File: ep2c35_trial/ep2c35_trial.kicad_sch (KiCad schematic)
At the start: 175 parts, among them J1 Conn_02x21_Odd_Even, J10 Conn_02x10_Odd_Even, J2 Conn_02x21_Odd_Even, J3 3M_8540-4500PL, J4 USB3_B_Micro_Amphenol_GSB343K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, J5 Conn_02x05_Odd_Even, J6 Conn_01x02_Male, J7 Conn_01x02_Male, J8 Conn_01x02_Male, J9 Conn_01x02_Male, U1 EP2C5F484, U10 SP3003-02UTG, U11 SP3003-02UTG, U12 SP3003-02UTG, U13 SP3003-02UTG, U14 SP3003-02UTG, U15 SP3003-02UTG, U16 SP3003-02UTG, U2 MIC37302, U3 FT600Q-B-T, U4 W25Q16JVSNIQ, U5 MIC39102, U6 MIC49150-1.2, U7 SP3003-02UTG, U8 SP3003-02UTG, U9 SP3003-02UTG, X1 FNETHE025, Y1 ABM7-30.000MHZ-D2Y-T

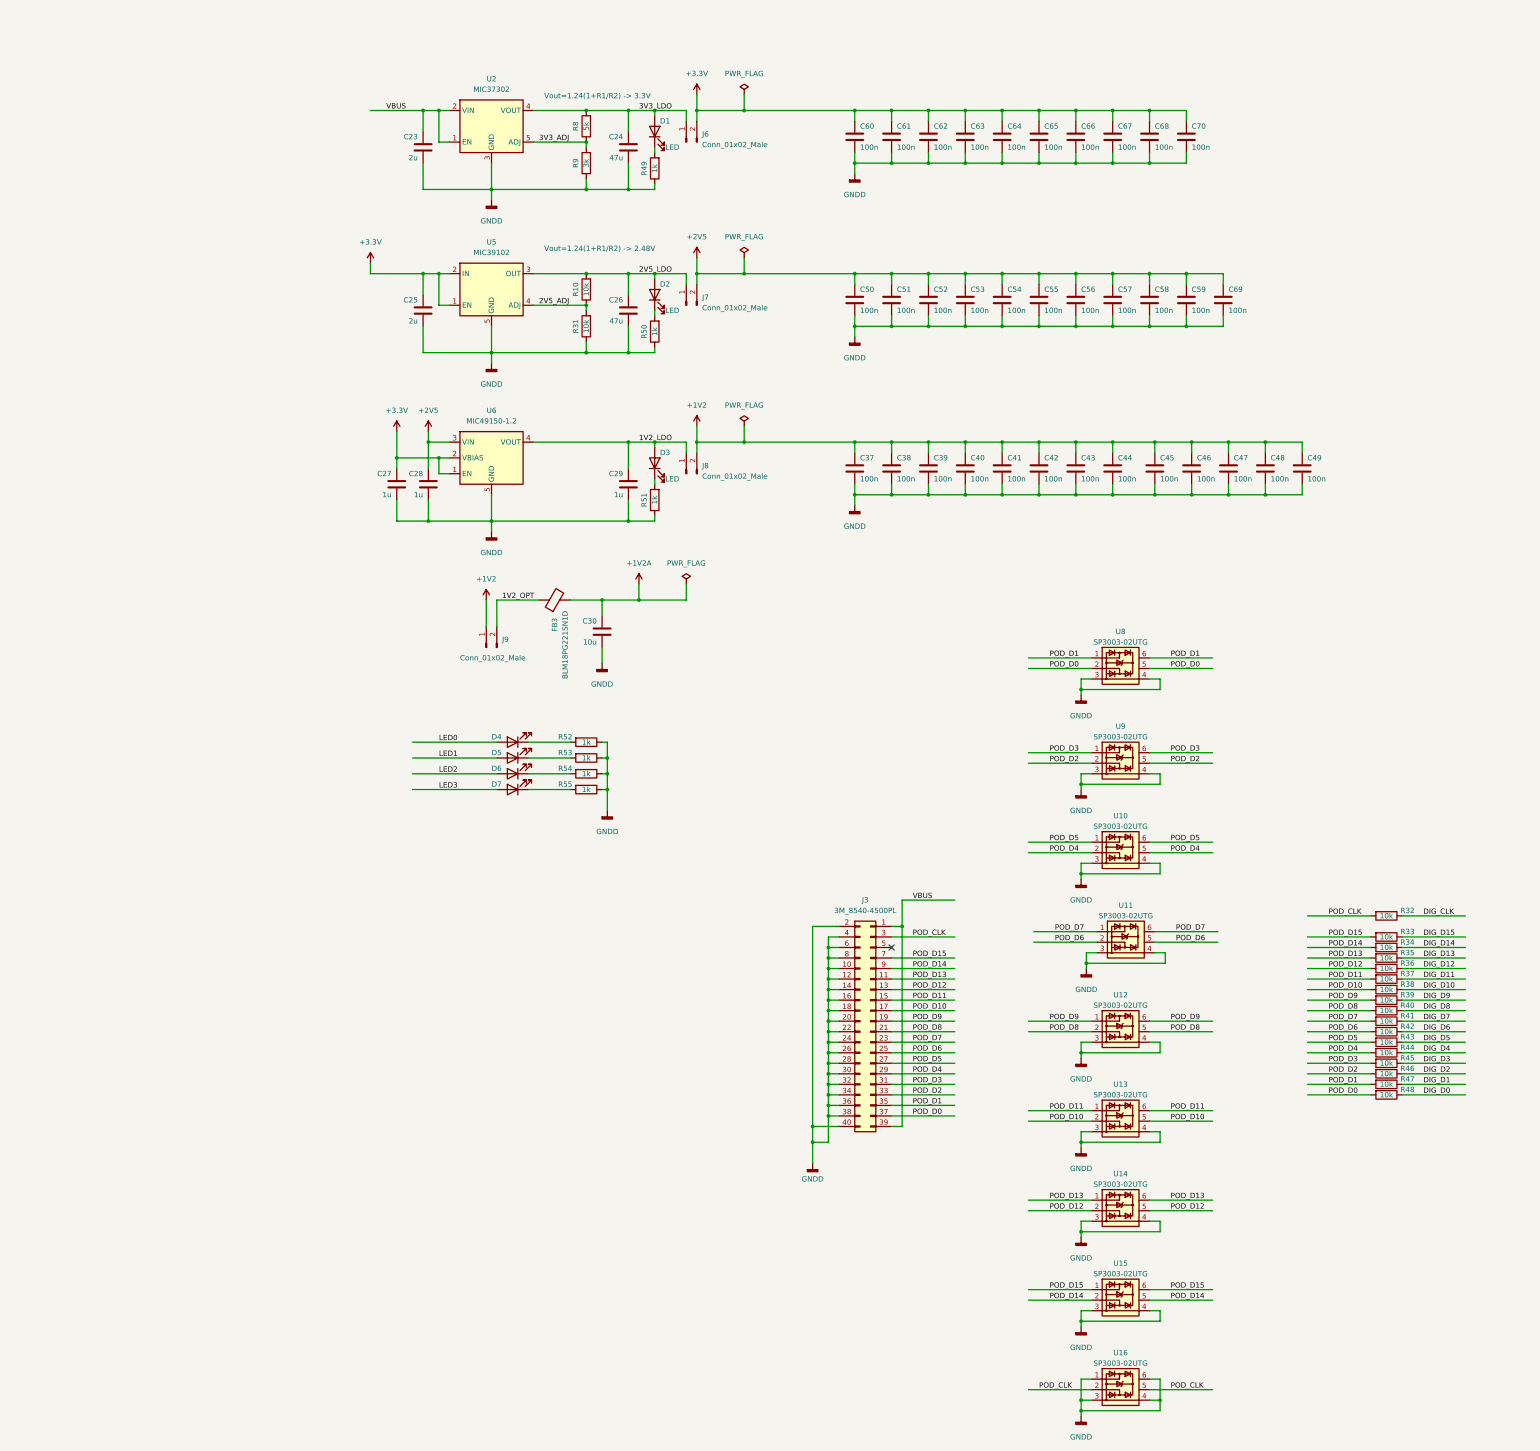
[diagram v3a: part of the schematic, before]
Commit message: Add LM317A power regulators.
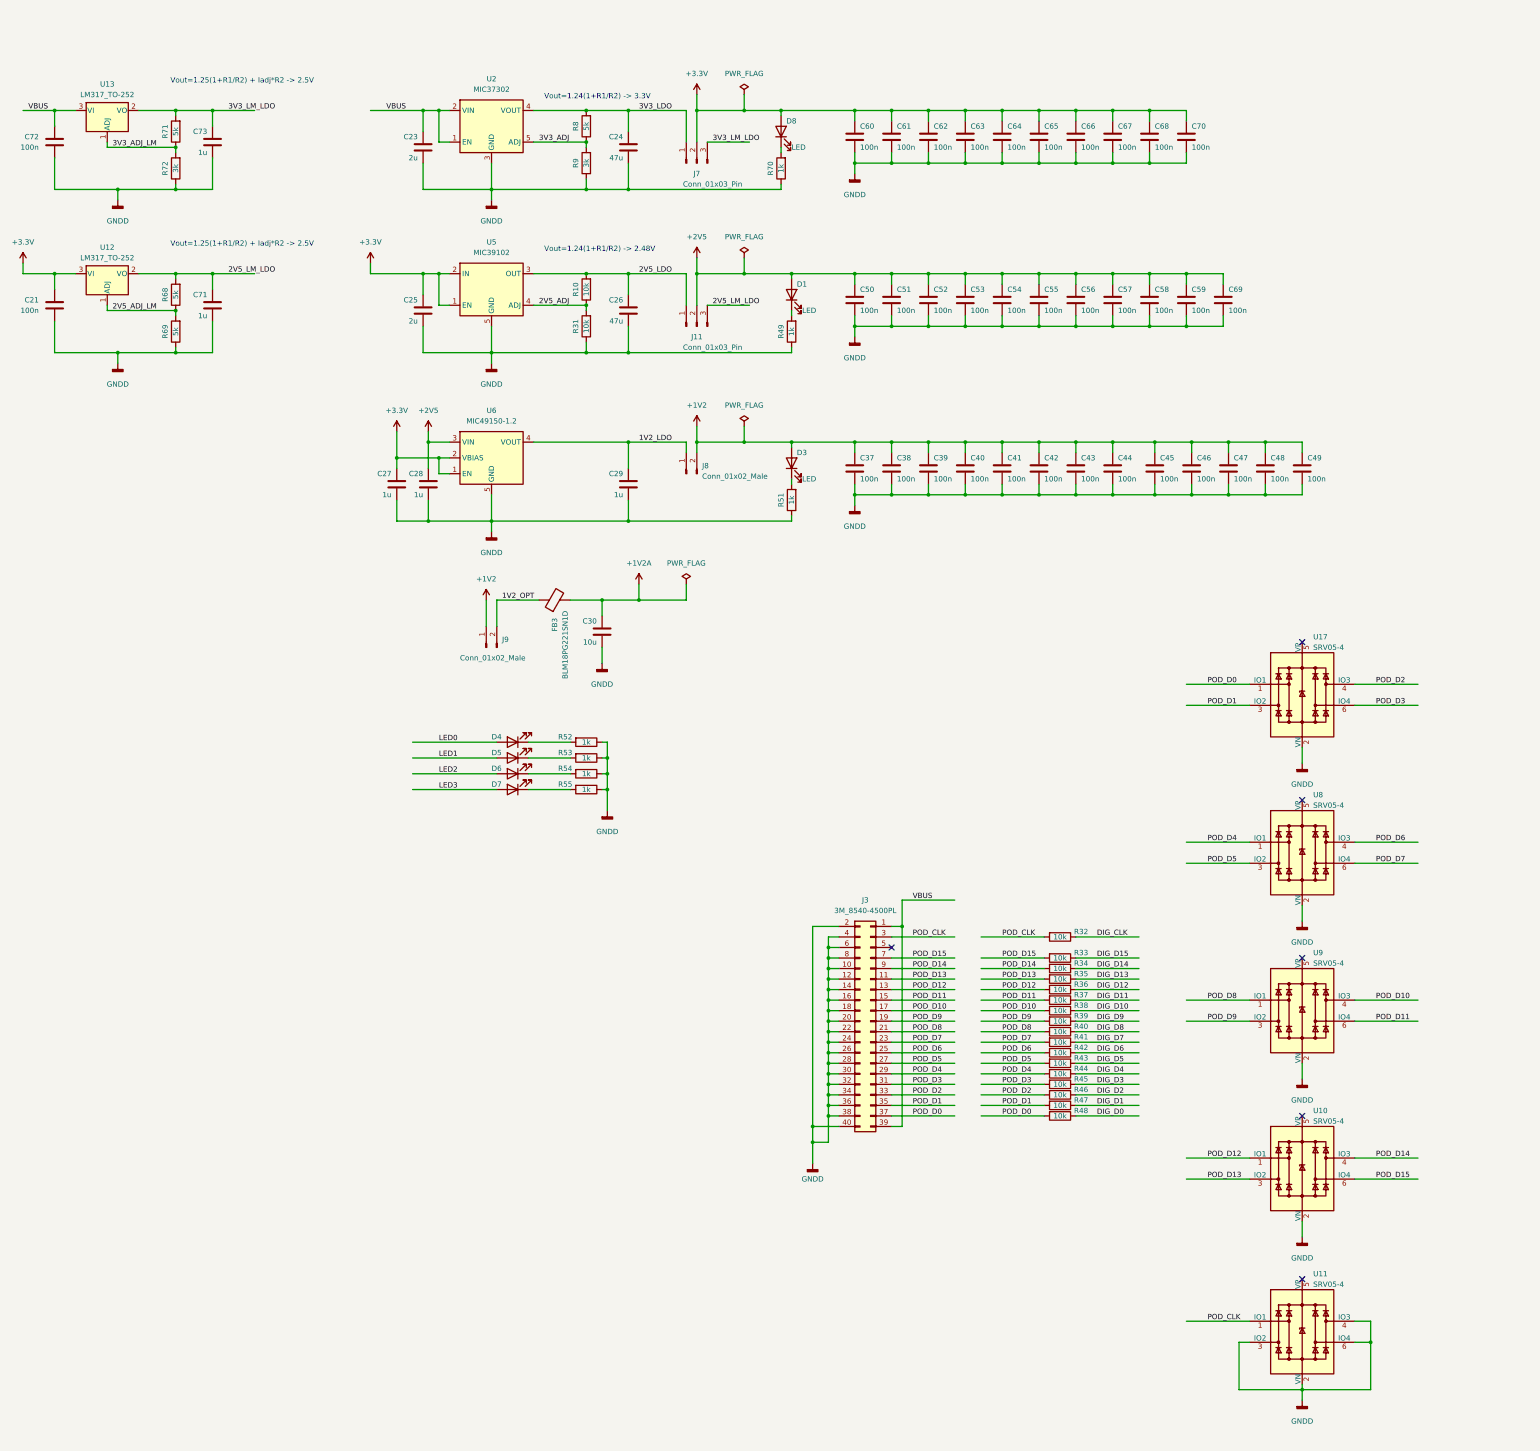
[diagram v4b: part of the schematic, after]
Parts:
- removed D2: LED, LED_SMD:LED_0603_1608Metric, symbol Device:LED
- removed J6, J7: Conn_01x02_Male, Connector_PinHeader_2.54mm:PinHeader_1x02_P2.54mm_Vertical, symbol Connector:Conn_01x02_Male
- removed R50: 1k, Resistor_SMD:R_0402_1005Metric, symbol Device:R
- removed U10, U11, U12, U13, U14, U15, U16, U8, U9: SP3003-02UTG, Package_TO_SOT_SMD:SOT-23-6, symbol logic_analyzer:SP3003-02UTG
- added C21, C72: 100n, Capacitor_SMD:C_0402_1005Metric, symbol Device:C
- added C71, C73: 1u, Capacitor_SMD:C_0805_2012Metric, symbol Device:C
- added D8: LED, LED_SMD:LED_0603_1608Metric, symbol Device:LED
- added J11, J7: Conn_01x03_Pin, Connector_PinHeader_2.54mm:PinHeader_1x03_P2.54mm_Vertical, symbol Connector:Conn_01x03_Pin
- added R68, R69, R71: 5k, Resistor_SMD:R_0402_1005Metric, symbol Device:R
- added R70: 1k, Resistor_SMD:R_0402_1005Metric, symbol Device:R
- added R72: 3k, Resistor_SMD:R_0402_1005Metric, symbol Device:R
- added U10, U11, U17, U8, U9: SRV05-4, Package_TO_SOT_SMD:SOT-23-6, symbol Power_Protection:SRV05-4
- added U12, U13: LM317_TO-252, Package_TO_SOT_SMD:TO-252-2, symbol Regulator_Linear:LM317_TO-252
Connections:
- net +1V2: now also D3.2 (A)
- net +2V5: now also D1.2 (A), J11.2 (Pin_2)
- net +3.3V: now also C21.1, D8.2 (A), J7.2 (Pin_2), U12.3 (VI)
- net 1V2_LDO: no longer D3.2 (A)
- net 2V5_LDO: now also J11.1 (Pin_1)
- net 3V3_LDO: now also J7.1 (Pin_1); no longer D1.2 (A)
- net GND: now also C21.2, C71.1, C72.2, C73.1, R69.1, R70.1, R72.1, U10.2 (VN), U11.2 (VN), U11.3 (IO2), U11.4 (IO3), U11.6 (IO4), U17.2 (VN), U8.2 (VN), U9.2 (VN)
- net POD_CLK: now also U11.1 (IO1)
- net POD_D0: now also U17.1 (IO1)
- net POD_D1: now also U17.3 (IO2)
- net POD_D10: now also U9.4 (IO3)
- net POD_D11: now also U9.6 (IO4)
- net POD_D12: now also U10.1 (IO1)
- net POD_D13: now also U10.3 (IO2)
- net POD_D14: now also U10.4 (IO3)
- net POD_D15: now also U10.6 (IO4)
- net POD_D2: now also U17.4 (IO3)
- net POD_D3: now also U17.6 (IO4)
- net POD_D4: now also U8.1 (IO1)
- net POD_D5: now also U8.3 (IO2)
- net POD_D6: now also U8.4 (IO3)
- net POD_D7: now also U8.6 (IO4)
- net POD_D8: now also U9.1 (IO1)
- net POD_D9: now also U9.3 (IO2)
- net VBUS: now also C72.1, U13.3 (VI)
- new net: D8.1 (K), R70.2
- new net 2V5_ADJ_LM: R68.1, R69.2, U12.1 (ADJ)
- new net 2V5_LM_LDO: C71.2, J11.3 (Pin_3), R68.2, U12.2 (VO)
- new net 3V3_ADJ_LM: R71.1, R72.2, U13.1 (ADJ)
- new net 3V3_LM_LDO: C73.2, J7.3 (Pin_3), R71.2, U13.2 (VO)
- no-connect marks 158 -> 163
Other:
- note added: "Vout=1.25(1+R1/R2) + Iadj*R2 -> 2.5V"
- moved on the sheet: D3, R32, R33, R34, R35, R36, R37, R38, R39, R40, R41, R42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

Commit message: Rename EP2C5 to EP2C35.
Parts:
- U1: value EP2C5F484 -> EP2C35F484; symbol Intel_FPGA:EP2C5F484 -> Intel_FPGA:EP2C35F484
